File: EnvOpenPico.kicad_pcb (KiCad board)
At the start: 2 copper layers, 21.1 x 51.3 mm, 33 parts, among them J2 Conn_01x02, J3 Conn_02x18_Odd_Even, J4 Conn_02x18_Odd_Even, J5 Conn_01x03_Male, U1 NCP1117-3.3_SOT223, U2 W25Q16JVSSIQ, U3 RP2040, X1 XO32

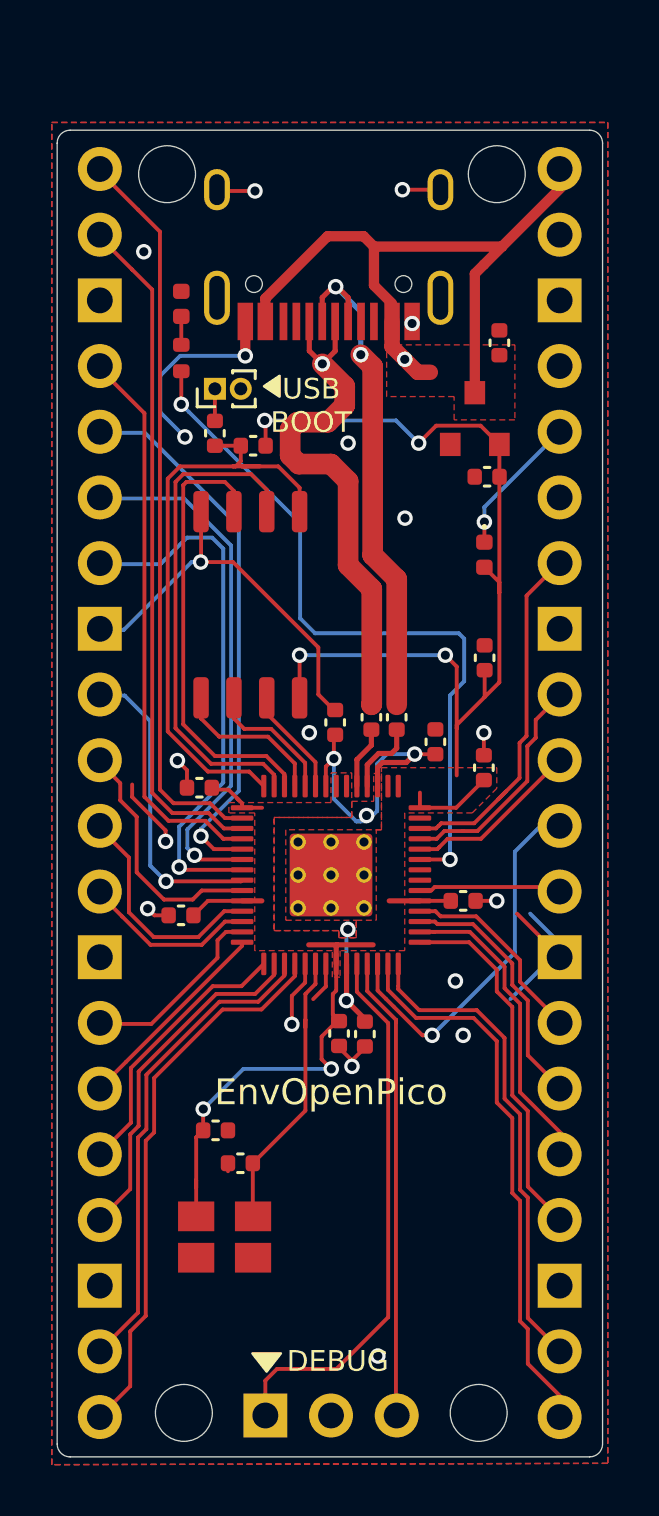
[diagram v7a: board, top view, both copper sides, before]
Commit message: Moved some vias to account for mechanical damage
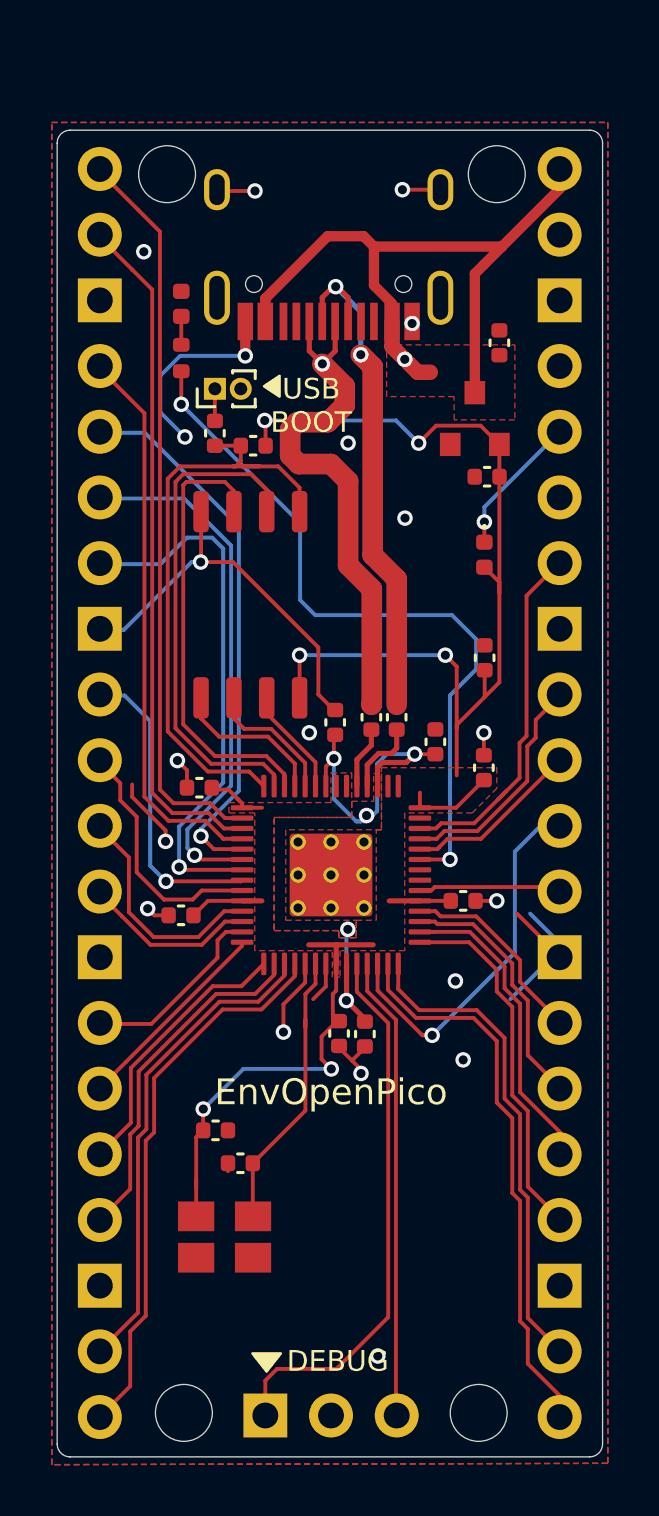
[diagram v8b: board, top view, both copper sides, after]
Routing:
- net GND: track 45.3 -> 46.2 mm
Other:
- board text added: "0.09mm width difference is needed for ground plane coverage"
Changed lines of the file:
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@@
     (44 Edge.Cuts user)
     (45 Margin user)
-    (46 B.CrtYd user)
-    (47 F.CrtYd user)
+    (46 B.CrtYd user hide)
+    (47 F.CrtYd user hide)
     (48 B.Fab user)
     (49 F.Fab user hide)
@@
     (pad_to_mask_clearance 0.051)
     (solder_mask_min_width 0.09)
-    (aux_axis_origin 98.925 50.2)
+    (aux_axis_origin 79 48)
     (visible_elements 7FFFFFFF)
     (pcbplotparams
@@
       (effects (font (size 1 1) (thickness 0.15)))
     )
-    (fp_text value Conn_02x18_Odd_Even (at 0 -50.59) (layer B.Fab)
-      (effects (font (size 1 1) (thickness 0.15)) (justify mirror))
+    (fp_text value Conn_02x18_Odd_Even (at 0 -50.59) (layer F.Fab)
+      (effects (font (size 1 1) (thickness 0.15)))
     )
     (fp_line (start -0.635 1.27) (end 1.27 1.27) (layer B.Fab) (width 0.1))
@@
     )
   )
+  (gr_text "0.09mm width difference is needed for ground plane coverage" (at 89.98 31.75) (layer Cmts.User)
+    (effects (font (size 1 1) (thickness 0.15)))
+  )
   (dimension 17.78 (width 0.15) (layer Dwgs.User)
     (gr_text "17.780 mm" (at 90.04 39.1) (layer Dwgs.User)
@@
     (arrow2b (pts (xy 98.93 40.4) (xy 97.803496 40.986421)))
   )
-  (target x (at 90.09 77.5) (size 1) (width 0.05) (layer Edge.Cuts))
   (gr_poly (pts (xy 87.5 58.6) (xy 88.1 58.2) (xy 88.1 59)) (layer F.SilkS) (width 0.1))
   (gr_text "VSYS is not implemented" (at 101.9 52.8) (layer Cmts.User)
@@
     (effects (font (size 1 1) (thickness 0.15)) (justify left))
   )
-  (gr_text "DO NOT CHANGE THE SIZE OF THE PCB OR THE PINOUT" (at 90.09 36.5) (layer Cmts.User)
+  (gr_text "DO NOT CHANGE THE SIZE OF THE PCB OR THE PINOUT" (at 123.76 29.11) (layer Cmts.User)
     (effects (font (size 1 1) (thickness 0.15)))
   )
@@
     (arrow2b (pts (xy 78.59 100) (xy 78.003579 98.873496)))
   )
-  (via (at 96.02 63.85) (size 0.6) (drill 0.35) (layers F.Cu B.Cu) (net 48))
   (via (at 93.225 56.175) (size 0.6) (drill 0.35) (layers F.Cu B.Cu) (net 1))
   (via (at 85.05 65.4) (size 0.6) (drill 0.35) (layers F.Cu B.Cu) (net 1))
   (via (at 96.5 78.5) (size 0.6) (drill 0.35) (layers F.Cu B.Cu) (net 1))
   (segment (start 96.5 78.5) (end 95.68 78.5) (width 0.15) (layer F.Cu) (net 1))
-  (via (at 90.9 84.9) (size 0.6) (drill 0.35) (layers F.Cu B.Cu) (net 1))
   (segment (start 90.6 83.91) (end 90.6 84.174998) (width 0.15) (layer F.Cu) (net 1))
   (segment (start 90.4 84.174998) (end 90.900002 84.675) (width 0.15) (layer F.Cu) (net 1))
   (segment (start 91.6 83.93) (end 91.6 84.175002) (width 0.15) (layer F.Cu) (net 1))
   (segment (start 91.4 84.175002) (end 90.900002 84.675) (width 0.15) (layer F.Cu) (net 1))
-  (segment (start 90.9 84.675002) (end 90.900002 84.675) (width 0.15) (layer F.Cu) (net 1))
-  (segment (start 90.9 84.9) (end 90.9 84.675002) (width 0.15) (layer F.Cu) (net 1))
   (via (at 94.9 81.6) (size 0.6) (drill 0.35) (layers F.Cu B.Cu) (net 1))
-  (via (at 95.2 83.7) (size 0.6) (drill 0.35) (layers F.Cu B.Cu) (net 1))
   (via (at 91.9 96.1) (size 0.6) (drill 0.35) (layers F.Cu B.Cu) (net 1))
   (segment (start 84.52 74.125) (end 84.52 73.444999) (width 0.15) (layer F.Cu) (net 1))
@@
   (segment (start 82.4 74.483808) (end 83.691928 75.775736) (width 0.15) (layer F.Cu) (net 1))
   (via (at 83.691928 76.2) (size 0.6) (drill 0.35) (layers F.Cu B.Cu) (net 1))
-  (via (at 88.575 83.275) (size 0.6) (drill 0.35) (layers F.Cu B.Cu) (net 1))
+  (segment (start 89.09 81.660736) (end 88.25 82.500736) (width 0.15) (layer F.Cu) (net 1))
   (segment (start 89.09 80.9375) (end 89.09 81.660736) (width 0.15) (layer F.Cu) (net 1))
-  (segment (start 89.09 81.660736) (end 88.575 82.175736) (width 0.15) (layer F.Cu) (net 1))
-  (segment (start 88.575 82.175736) (end 88.575 83.275) (width 0.15) (layer F.Cu) (net 1))
+  (segment (start 88.25 82.500736) (end 88.25 83.575) (width 0.15) (layer F.Cu) (net 1))
+  (via (at 88.25 83.575) (size 0.6) (drill 0.35) (layers F.Cu B.Cu) (net 1))
+  (via (at 95.2 84.65) (size 0.6) (drill 0.35) (layers F.Cu B.Cu) (net 1))
+  (via (at 91.25 85.175) (size 0.6) (drill 0.35) (layers F.Cu B.Cu) (net 1))
+  (segment (start 90.900002 84.675) (end 91.25 85.024998) (width 0.15) (layer F.Cu) (net 1))
+  (segment (start 91.25 85.024998) (end 91.25 85.175) (width 0.15) (layer F.Cu) (net 1))
   (segment (start 98.99 50.2) (end 98.99 50.91) (width 0.15) (layer F.Cu) (net 2))
   (segment (start 98.99 50.91) (end 96.7 53.2) (width 0.4) (layer F.Cu) (net 2))
@@
   (segment (start 84.3 59.3) (end 84.3 58.02) (width 0.15) (layer F.Cu) (net 27))
   (segment (start 88.895 63.895) (end 84.599999 59.599999) (width 0.15) (layer B.Cu) (net 27))
-  (segment (start 88.895 67.575) (end 88.895 63.895) (width 0.15) (layer B.Cu) (net 27))
-  (segment (start 89.474998 68.154998) (end 88.895 67.575) (width 0.15) (layer B.Cu) (net 27))
-  (segment (start 95.24 68.362996) (end 95.032002 68.154998) (width 0.15) (layer B.Cu) (net 27))
+  (segment (start 88.895 66.865) (end 88.895 63.895) (width 0.15) (layer B.Cu) (net 27))
+  (segment (start 89.48 67.45) (end 88.895 66.865) (width 0.15) (layer B.Cu) (net 27))
+  (segment (start 95.7 68.38) (end 94.77 67.45) (width 0.15) (layer B.Cu) (net 27))
+  (segment (start 94.77 67.45) (end 89.48 67.45) (width 0.15) (layer B.Cu) (net 27))
+  (segment (start 94.69 70.557003) (end 95.7 69.547003) (width 0.15) (layer B.Cu) (net 27))
   (segment (start 84.599999 59.599999) (end 84.3 59.3) (width 0.15) (layer B.Cu) (net 27))
-  (segment (start 95.24 70.007003) (end 95.24 68.362996) (width 0.15) (layer B.Cu) (net 27))
-  (segment (start 95.032002 68.154998) (end 89.474998 68.154998) (width 0.15) (layer B.Cu) (net 27))
-  (segment (start 94.69 70.557003) (end 95.24 70.007003) (width 0.15) (layer B.Cu) (net 27))
+  (segment (start 95.7 69.547003) (end 95.7 68.38) (width 0.15) (layer B.Cu) (net 27))
   (segment (start 94.69 76.9) (end 94.69 70.557003) (width 0.15) (layer B.Cu) (net 27))
   (segment (start 94.10001 77.96499) (end 98.81499 77.96499) (width 0.15) (layer F.Cu) (net 28))
@@
   (segment (start 92.63 70.92) (end 92.63 66.058248) (width 0.8) (layer F.Cu) (net 47))
   (segment (start 92.63 66.058248) (end 91.7 65.128248) (width 0.8) (layer F.Cu) (net 47))
+  (via (at 96.02 63.85) (size 0.6) (drill 0.35) (layers F.Cu B.Cu) (net 48))
   (segment (start 96.02 63.27) (end 96.02 63.85) (width 0.15) (layer B.Cu) (net 48))
   (segment (start 98.93 60.36) (end 96.02 63.27) (width 0.15) (layer B.Cu) (net 48))
